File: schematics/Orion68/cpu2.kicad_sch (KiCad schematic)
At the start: 32 parts, among them J4 clock, J5 clock1, J6 Euro96pin, Q5 2N3904, Q6 2N3904, SW1 sw_reset, U16 74LS393, U2.1 68000D, U2.2 74LS138, U2.? ATmega8-16P, U21_C? 100nF, U3.? 74LS138

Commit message: New cpu board with NMOS running
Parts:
- added J10: Conn_02x08_Counter_Clockwise, symbol Connector_Generic:Conn_02x08_Counter_Clockwise
- added unit 3 of U16
- added U19, U20: 74HC74, Package_DIP:DIP-14_W7.62mm, symbol 74xx:74HC74
- added U21: 74HC14, symbol 74xx:74HC14
- added U22: 74HC164, symbol 74xx:74HC164
- R23, R24, R25, R26, R27, R28, R29, R30: value 10k -> 1k5
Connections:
- net C.R/W is gone; now on net R/W: U2.1.9 (R/W)
- net +5V: now also CU21_C?.1, R23.2, R24.2, R25.2, R26.2, R27.2, R28.2, R29.2, R30.2, U2.1.14 (VCC), U2.1.49 (VCC), U21_C?.1, U19.1 (~{R}), U19.4 (~{S}), U20.1 (~{R}), U22.1 (DSA), U22.14 (VCC), U22.2 (DSB)
- net 4MHZ: now also U19.3 (C), U22.8 (CP)
- net BOOTIN: now also U20.5 (Q)
- net GND: now also U20.2 (D), U22.7 (GND)
- net IPL0: no longer R30.2, U2.1.25 (IPL0)
- net IPL1: no longer R29.2, U2.1.24 (IPL1)
- net IPL2: no longer R28.2, U2.1.23 (IPL2)
- net /BERR: now also R24.1, U2.1.22 (BERR)
- net /RESET: now also U20.4 (~{S})
- net /VPA: now also R25.1; no longer R25.2
- net B/cpurd renamed /cpurd
- net /cpurd: now also U21.2
- net B/cpuwr renamed R/W
- net R/W: now also U21.1
- net C.E: no longer names the net of U2.1.20 (E)
- net C.FC0: no longer names the net of U2.1.28 (FC0)
- net C.FC1: no longer names the net of U2.1.27 (FC1)
- net C.FC2: no longer names the net of U2.1.26 (FC2)
- net C./AS renamed /AS
- net /AS: now also U19.2 (D), U21.5
- removed net C./BERR: R24.2, U2.1.22 (BERR)
- net C./BG: no longer names the net of U2.1.11 (BG)
- net C./BGACK renamed /BGACK
- net /BGACK: now also R27.1; no longer R27.2
- net C./BR renamed /BR
- net /BR: now also R26.1; no longer R26.2
- net C./DTACK renamed /DTACK
- net /DTACK: now also R23.1, U19.5 (Q), U21.4; no longer R23.2
- net C./LDS renamed /LDS
- net C./UDS renamed /UDS
- net C./VMA: no longer names the net of U2.1.19 (VMA)
- new net: U21.6, U22.9 (~{MR})
- new net: J10.1 (Pin_1), U22.3 (Q0)
- new net: J10.10 (Pin_10), J10.11 (Pin_11), J10.12 (Pin_12), J10.13 (Pin_13), J10.14 (Pin_14), J10.15 (Pin_15), J10.16 (Pin_16), J10.9 (Pin_9), U21.3
- new net: J10.2 (Pin_2), U22.4 (Q1)
- new net: J10.3 (Pin_3), U22.5 (Q2)
- new net: J10.4 (Pin_4), U22.6 (Q3)
- new net: J10.5 (Pin_5), U22.10 (Q4)
- new net: J10.6 (Pin_6), U22.11 (Q5)
- new net: J10.7 (Pin_7), U22.12 (Q6)
- new net: J10.8 (Pin_8), U22.13 (Q7)
- new net /IPL0: R30.1, U2.1.25 (IPL0)
- new net /IPL1: R29.1, U2.1.24 (IPL1)
- new net /IPL2: R28.1, U2.1.23 (IPL2)
- new net /KILLBT: U20.3 (C)
- no-connect marks 0 -> 1
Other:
- moved on the sheet: CU21_C?, D?, J6, R23, R24, R25, R26, R27, R28, R29, R30, R?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

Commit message: Updating...
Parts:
- removed U2.2: 74LS138, symbol 74xx:74LS138
- added unit 3 of U602
- gave numbers to parts that had none: 3
- renumbered J6 to J600, J4 to J601, J5 to J602, R30 to R600, R29 to R601, R28 to R602, R27 to R603, R26 to R604, R25 to R605, R24 to R606, R23 to R607, U2.1 to U600, U16 to U601, U19 to U602, U20 to U602, U21 to U603, Y1 to Y600
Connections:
- net +5V: now also U602.13 (~{R}), U604.20 (AVCC), U604.21 (AREF); no longer U602.1 (~{R})
- net BOOTIN: now also U602.9 (Q); no longer U602.5 (Q)
- net GND: now also U602.12 (D), U604.22 (AGND), U604.8 (GND); no longer U602.2 (D)
- net RESET: now also U603.8
- net /KILLBT: now also U602.11 (C); no longer U602.3 (C)
- net /RESET: now also U602.10 (~{S}), U603.9, U604.1 (PC6/~{RESET}); no longer U602.4 (~{S})
- net /IO_CS: no longer names the net of J600.85
- net /RAM_CS: no longer names the net of J600.84
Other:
- note added: "600"
- moved on the sheet: CU600_1, CU600_2, D?, R600, R601, R602, R603, R604, R605, R606, R607, R?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

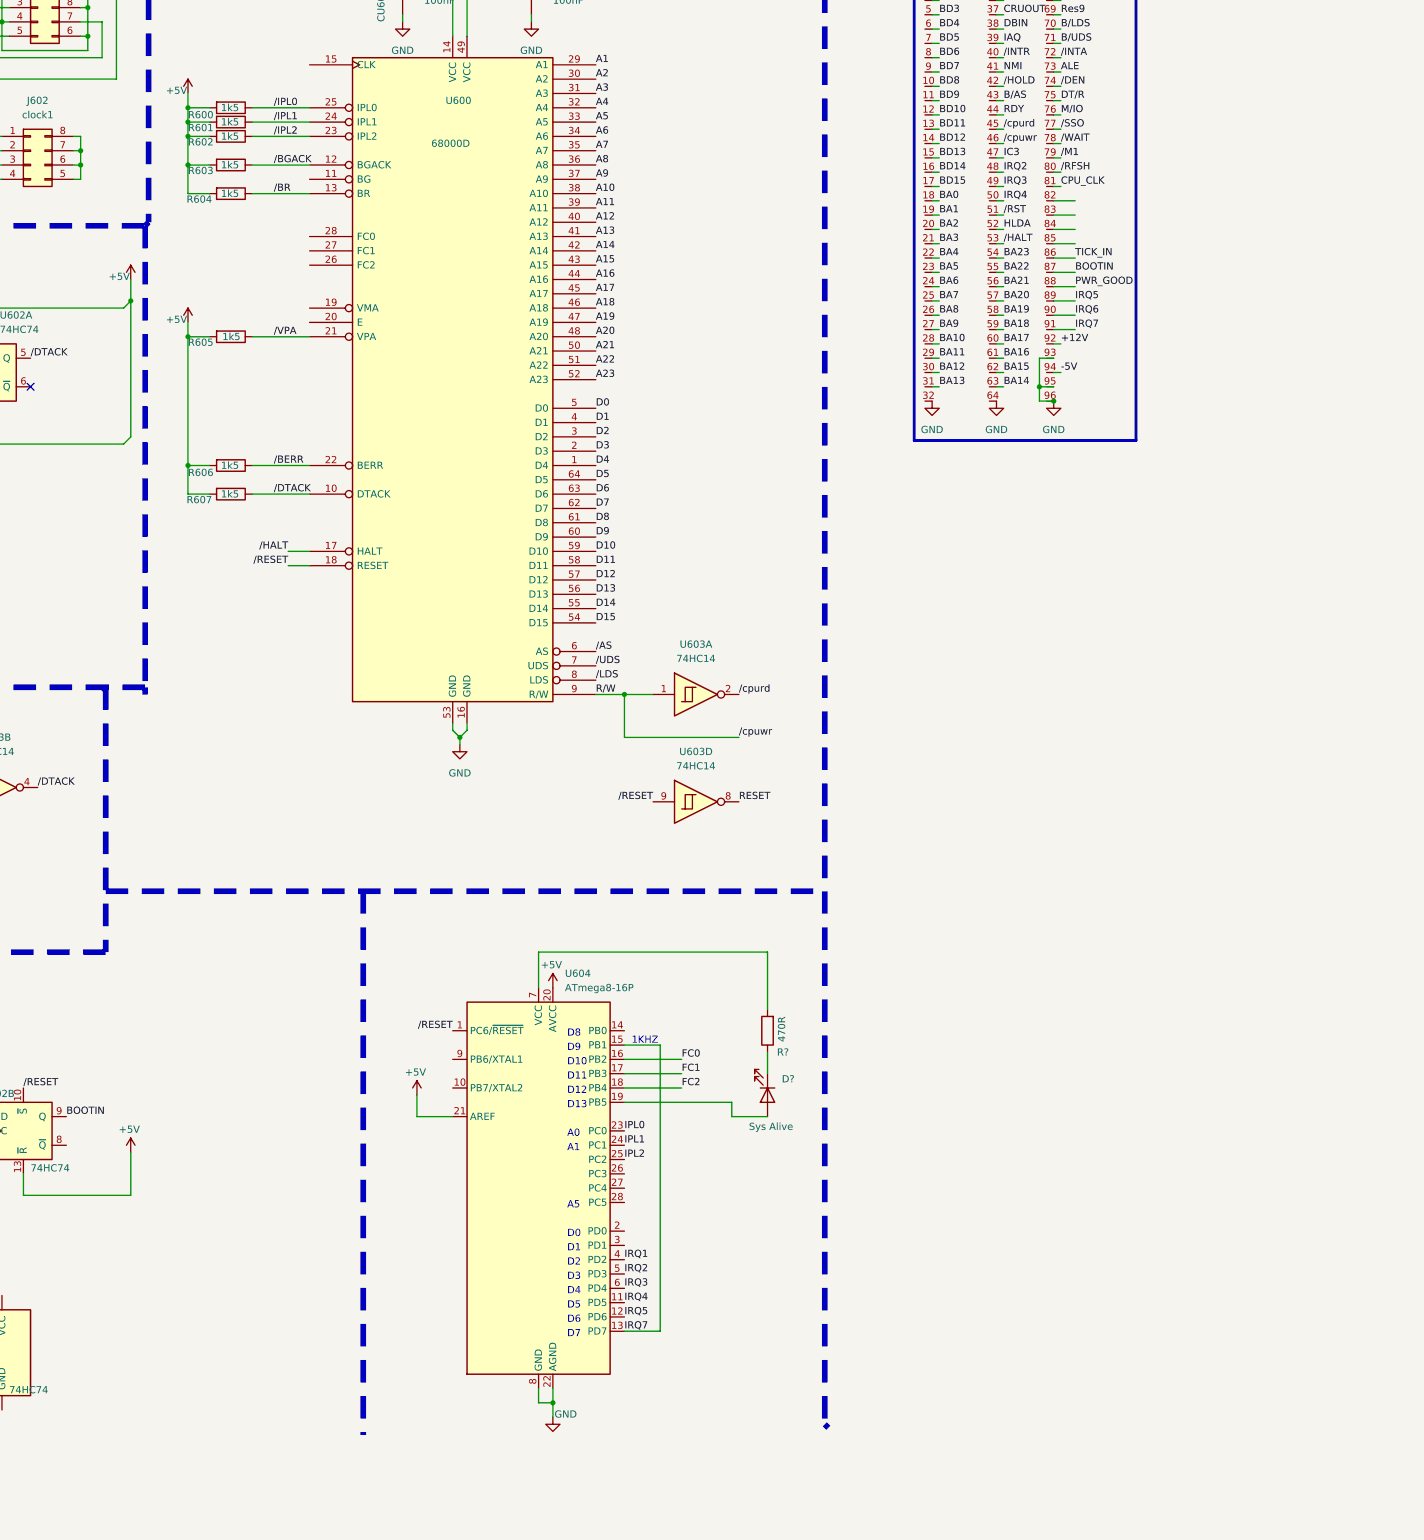
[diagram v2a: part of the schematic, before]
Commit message: A20 bug fixed, missing serial CSA, running ok
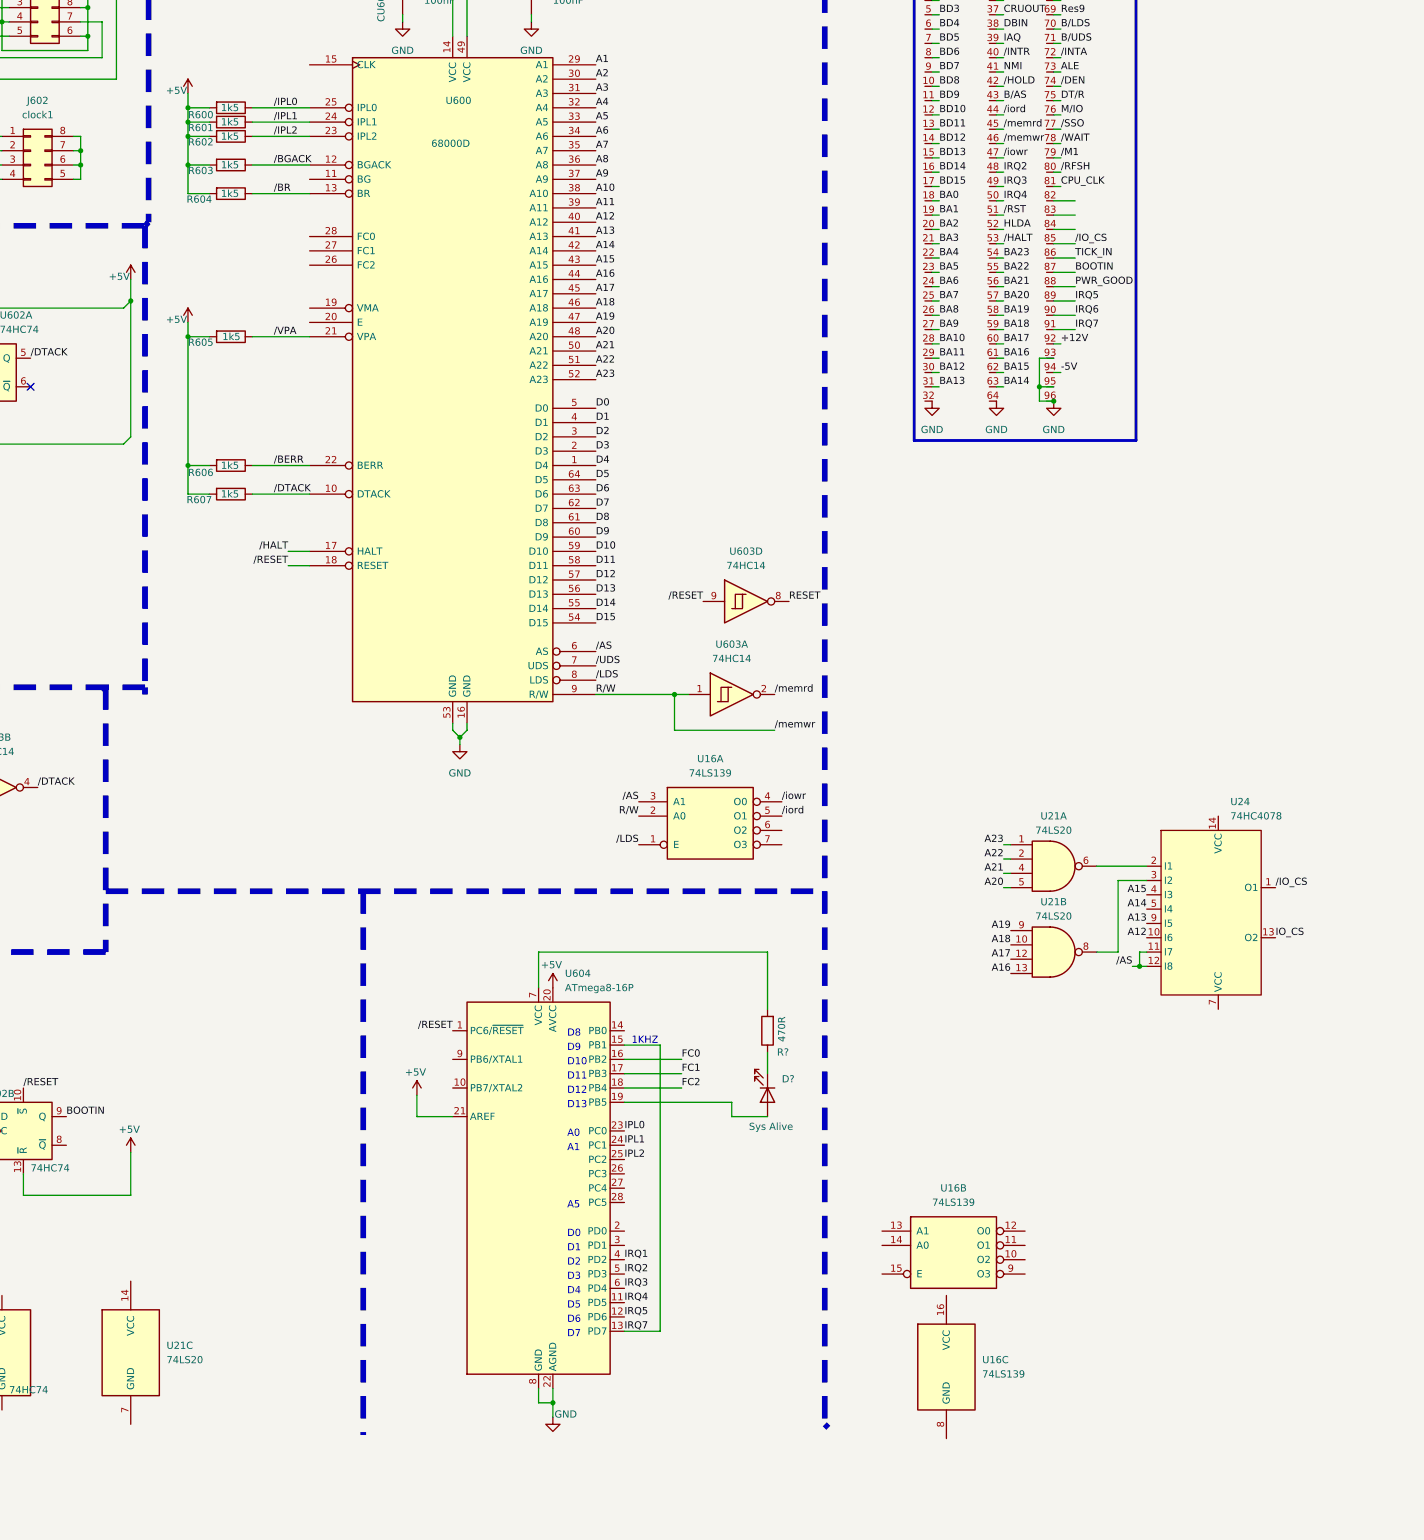
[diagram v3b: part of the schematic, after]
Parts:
- added U16: 74LS139, symbol 74xx:74LS139
- added U21: 74LS20, symbol 74xx:74LS20
- added U24: 74HC4078, symbol pdSilva:74HC4078
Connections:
- net A12: now also U24.10 (I6)
- net A13: now also U24.9 (I5)
- net A14: now also U24.5 (I4)
- net A15: now also U24.4 (I3)
- net A16: now also U21.13
- net A17: now also U21.12
- net A18: now also U21.10
- net A19: now also U21.9
- net A20: now also U21.5
- net A21: now also U21.4
- net A22: now also U21.2
- net A23: now also U21.1
- net R/W: now also U16.2 (A0)
- net /AS: now also U16.3 (A1), U24.11 (I7), U24.12 (I8)
- net /LDS: now also U16.1 (E)
- net /IO_CS: now reaches J600.85
- net /IO_CS: now also U24.1 (O1)
- net IC3 renamed /iowr
- net /iowr: now also U16.4 (O0)
- net RDY renamed /iord
- net /iord: now also U16.5 (O1)
- net /cpurd renamed /memrd
- new net: U21.6, U24.2 (I1)
- new net: U21.8, U24.3 (I2)
- new net IO_CS: U24.13 (O2)
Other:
- moved on the sheet: U603A, U603D

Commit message: updating
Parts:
- removed U3.?: 74LS138, symbol 74xx:74LS138
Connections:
- net A12: no longer U24.10 (I6)
- net A13: no longer U24.9 (I5)
- net A14: no longer U24.5 (I4)
- net A15: no longer U24.4 (I3)
- net A16: now also U21.9; no longer U21.13
- net A17: now also U21.10; no longer U21.12
- net A18: now also U21.12; no longer U21.10
- net A19: now also U21.13; no longer U21.9
- net A21: now also U24.4 (I3)
- net A22: now also U24.3 (I2)
- net A23: now also U24.2 (I1)
- net /AS: no longer U24.11 (I7), U24.12 (I8)
- net /IO_CS: now also J600.84, U21.6; no longer J600.85, U24.1 (O1)
- net /IO_CS1: now reaches J600.82
- net /IO_CS1: now also U21.8
- net /UART_CS: now reaches J600.83
- net at U24.7 (VCC): now also U24.10 (I6), U24.11 (I7), U24.12 (I8), U24.5 (I4), U24.9 (I5)
- net IO_CS: no longer names the net of U24.13 (O2)
- new net /MEM_CS: J600.85, U24.1 (O1)
- no-connect marks 1 -> 2
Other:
- note added: "NÃO IMPLEMENTADO AINDA"
- moved on the sheet: U16B, U16C, U21A, U21B, U24, U602B, U603E, U603F
